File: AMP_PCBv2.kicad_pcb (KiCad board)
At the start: 2 copper layers, 100.1 x 100.1 mm, 114 parts, among them J1 POWER, J2 EBRAKE, J3 MC, J4 STEERING, J5 OLED Breakout, J6 EBRAKE_BREAKOUT, Q1 Q_NMOS_GDS, Q2 Q_NMOS_GDS, Q3 Q_NMOS_GDS, Q4 Q_NMOS_GDS, U1 Teensy4.0, U10 RFM9x, U2 FT234XD, U3 LM1117-ADJ, U4 LM1117-ADJ, U5 74HC157, U6 74HC157, U7 74HC4060, U8 74HC00, U9 TLV272

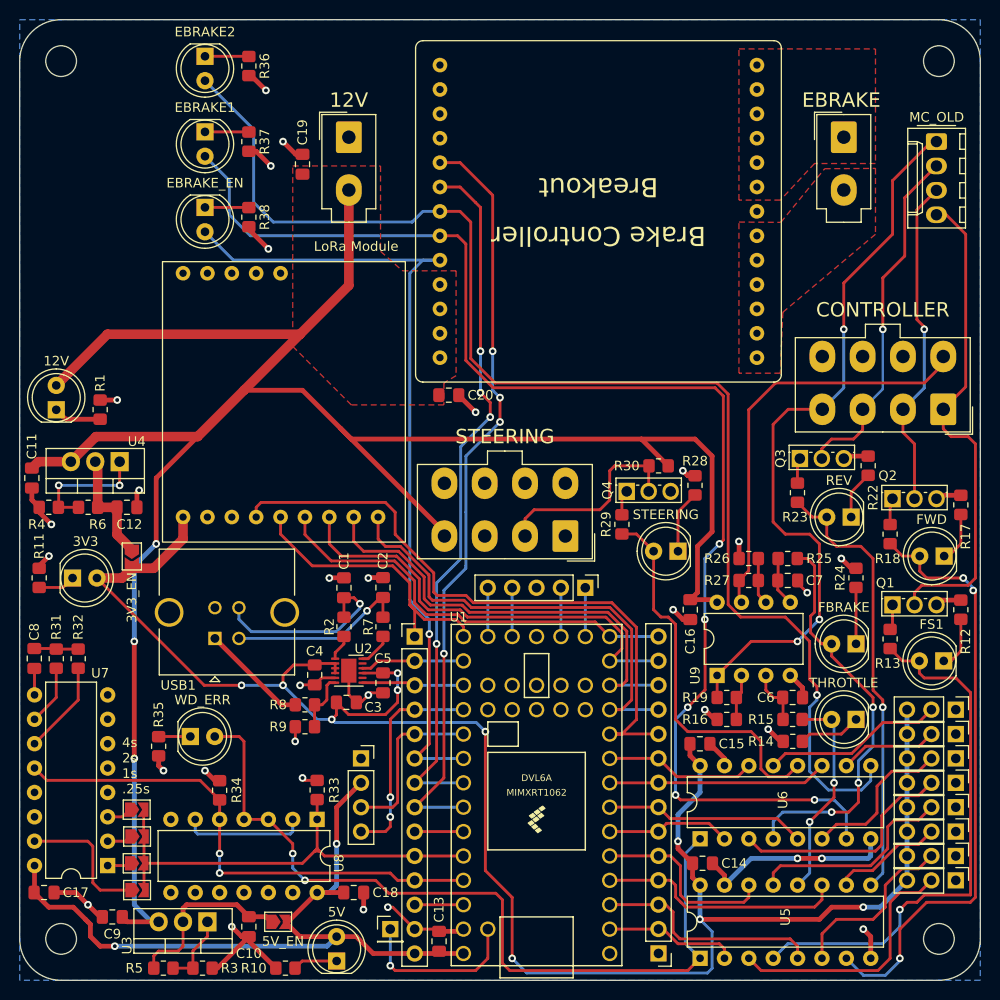
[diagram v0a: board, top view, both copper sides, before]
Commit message: Add extra error LED
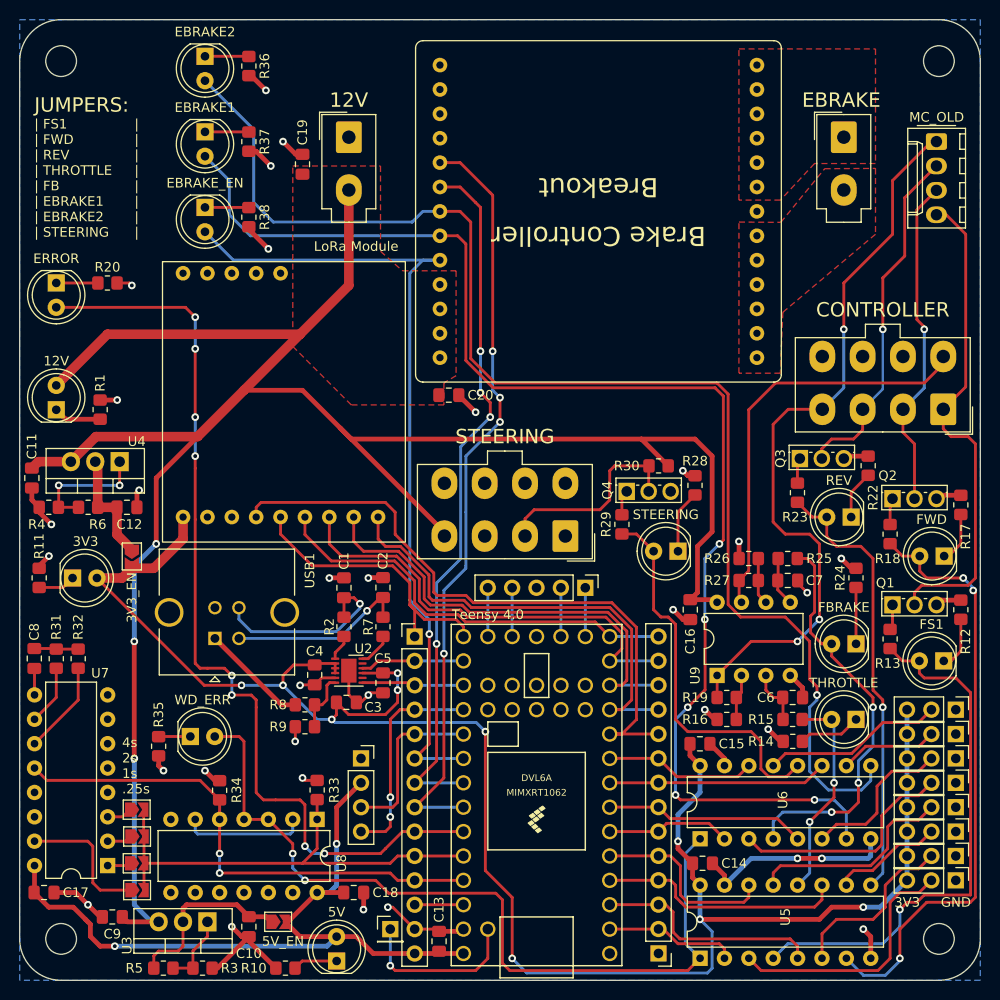
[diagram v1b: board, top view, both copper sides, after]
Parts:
- added D14: RD, LED_THT:LED_D5.0mm, F.Cu at (91.2, 74.9)
- added R20: 33, Resistor_SMD:R_0805_2012Metric_Pad1.20x1.40mm_HandSolder, F.Cu at (96.5, 74.9)
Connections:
- net Net-(JT3-Pad9) renamed /ERR_OTHER
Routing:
- net /ERR_OTHER: track 5.08 -> 97.4 mm, vias 0 -> 8
- net Net-(D14-Pad1): track 0.00 -> 4.34 mm
- net GND: track 124.1 -> 125.8 mm, vias 31 -> 32
- net /WD_SET: track 48.3 -> 49.3 mm
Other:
- board text added: "ERROR"
- board text added: "GND"
- board text added: "JUMPERS:"
- board text added: "Teensy 4.0"
- board text added: "| FS1 | FWD | REV | THROTTLE | FB | EBRAKE1 | EBRAKE2 | STEERING"
- board text added: "| | | | | | | |"

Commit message: Fix #3
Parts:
- moved C18 21.9 mm to (104.1, 126.0)
- moved R33 17.6 mm to (104.1, 138.2), turned to 0 degrees
- moved U8 16.1 mm to (103.1, 135.9), turned to 90 degrees
- moved R34 11.2 mm to (112.3, 138.2), turned to 180 degrees
- moved R35 9.32 mm to (111.0, 121.4)
- moved D13 2.17 mm to (105.9, 120.1), turned to -90 degrees
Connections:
- C17 pad 1: +5V -> +3V3
- C18 pad 1: +5V -> +3V3
- U7 pad 16: +5V -> +3V3
- U8 pad 14: +5V -> +3V3
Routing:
- net +3V3: track 198.4 -> 254.0 mm, vias 10 -> 14
- net +5V: track 79.4 -> 40.0 mm
- net /ERR_OTHER: track 97.4 -> 92.7 mm, vias 8 -> 7
- net /WD_SET: track 49.3 -> 47.1 mm, vias 0 -> 2
- net /LORA_MOSI: track 47.0 -> 45.0 mm
- net Net-(D13-Pad1): track 3.31 -> 5.19 mm
- net /LORA_CS: track 48.4 -> 46.6 mm
- net /WD_SEL: track 85.5 -> 87.3 mm, vias 2 -> 1
- net /LORA_RST: track 49.1 -> 47.4 mm
- net /LORA_MISO: track 44.4 -> 43.0 mm
- net /LORA_INT: track 66.9 -> 65.7 mm
- net /WD_RESET: track 54.0 -> 55.1 mm, vias 2 -> 3
- net /LORA_SCK: track 30.7 -> 30.0 mm
- net Net-(U8-Pad2): track 12.9 -> 12.2 mm, vias 0 -> 2
- net GND: track 125.8 -> 125.9 mm, vias 32 -> 31
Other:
- board text added: "AMP PCBv2 Revision A 2022-12-27"
- board text removed: "AMP PCBv2 Revision A 2022-12-26"
